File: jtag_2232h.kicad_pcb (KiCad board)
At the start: 2 copper layers, 60 x 25 mm, 90 parts

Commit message: Another import attempt.
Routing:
- added copper zone on F.Cu, net (none)
- removed copper zone on F.Cu, net NetCONN_USB_SHELL

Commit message: Annotated with modified KiCAD
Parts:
- CONN_JTAG: value (none) -> HDR_2x6
- CONN_USB: value (none) -> MICRO_USB_B
- C_BYP_LDO_V1P8: value (none) -> 22nF
- C_EEPROM_VCC, C_EPLD_V1P8_1, C_EPLD_V1P8_2, C_EPLD_VCC_1, C_EPLD_VCC_2, C_FT_CORE_1, C_FT_CORE_2, C_FT_CORE_3, C_FT_VCC_1, C_FT_VCC_2, C_FT_VCC_3, C_FT_VCC_4: value (none) -> 1uF
- C_EPLD_VEIO_1, C_EPLD_VEIO_2, C_OPAMP, C_VEIO_FB: value (none) -> 100nF
- C_FT_OSC_IN, C_FT_OSC_OUT: value (none) -> 4pF
- C_FT_PHY, C_FT_PLL, C_FT_REG_OUT: value (none) -> 3.3uF
- C_IN_LDO_VCC: value (none) -> 2.2uF
- C_OUT_LDO_VCC, C_VEIO_OUT: value (none) -> 10uF
- C_VEIO_CMP: value (none) -> 100pF
- D_JTAG_1, D_JTAG_2, D_JTAG_3, D_JTAG_4, D_JTAG_5: value (none) -> DIODE_2_CC
- EPRG_FT_TCK, EPRG_TCK, EPRG_TDI, EPRG_TDO, EPRG_TMS, GND, UDM, UDN, UGND, V1P8, VBUS, VCC, VCORE, VEIO, VIIO: value (none) -> Test_Point
- LED_FN, LED_PWR: value (none) -> LED_2
- Q_LDO, Q_OV: value (none) -> BJT_PNP
- Q_PWR_LED: value (none) -> MOSFET_P
- Q_TPWR: value (none) -> BJT_NPN
- R_EIO_BYPASS, R_EPRG_EN, R_FT_LDO, R_FT_PHY, R_FT_PLL, R_USB_GND: value (none) -> 0Ohm
- R_EPRG_TCK_PULL, R_PWR_LED_PULL, R_SER_LED_PULL, R_SPI: value (none) -> 10kOhm
- R_FT_REF: value (none) -> 12kOhm
- R_FT_RESET, R_TPWR: value (none) -> 1kOhm
- R_GND_DETECT_PULL: value (none) -> 47kOhm
- R_JTAG_1, R_JTAG_2, R_JTAG_3: value (none) -> 180Ohm
- R_LED_FN, R_LED_PWR: value (none) -> 330Ohm
- R_OUT_LDO_VCC: value (none) -> 2.2Ohm
- R_QBASE: value (none) -> 47Ohm
- R_SPI_DO: value (none) -> 2.2kOhm
- R_VEIO_CMP: value (none) -> 56kOhm
- R_VEIO_DN: value (none) -> 1MOhm
- R_VEIO_FB: value (none) -> 49.9kOhm
- R_VEIO_IN: value (none) -> 200kOhm
- TVS_JTAG_1, TVS_JTAG_2, TVS_JTAG_3: value (none) -> ESD5V0S4US
- U_EEPROM: value (none) -> SPI_EEPROM
- U_EPLD: value (none) -> 5M40Z
- U_FTDI: value (none) -> FT2232H
- U_LDO_V1P8: value (none) -> LDO_SOT23
- U_LDO_VCC: value (none) -> LDO_1117
- U_OPAMP: value (none) -> MCP6001
- Y_FTDI: value (none) -> XTAL_4P
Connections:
- net EPRG_FT_TCK renamed /EPRG_FT_TCK
- net EPRG_TCK renamed /EPRG_TCK
- net EPRG_TDI renamed /EPRG_TDI
- net EPRG_TDO renamed /EPRG_TDO
- net EPRG_TMS renamed /EPRG_TMS
- net FT_GPIO_H0 renamed /FT_GPIO_H0
- net FT_GPIO_H1 renamed /FT_GPIO_H1
- net FT_GPIO_H2 renamed /FT_GPIO_H2
- net FT_GPIO_H3 renamed /FT_GPIO_H3
- net FT_GPIO_H4 renamed /FT_GPIO_H4
- net FT_GPIO_H5 renamed /FT_GPIO_H5
- net FT_GPIO_H6 renamed /FT_GPIO_H6
- net FT_GPIO_H7 renamed /FT_GPIO_H7
- net FT_GPIO_L0 renamed /FT_GPIO_L0
- net FT_GPIO_L1 renamed /FT_GPIO_L1
- net FT_GPIO_L2 renamed /FT_GPIO_L2
- net FT_JTAG_EN_N renamed /FT_JTAG_EN_N
- net FT_JTAG_RTCK renamed /FT_JTAG_RTCK
- net FT_JTAG_TCK renamed /FT_JTAG_TCK
- net FT_JTAG_TDI renamed /FT_JTAG_TDI
- net FT_JTAG_TDO renamed /FT_JTAG_TDO
- net FT_JTAG_TMS renamed /FT_JTAG_TMS
- net FT_SER_LED renamed /FT_SER_LED
- net FT_SER_RXD renamed /FT_SER_RXD
- net FT_SER_TXD renamed /FT_SER_TXD
- net GND_DETECT renamed /GND_DETECT
- net JTAG_RST renamed /JTAG_RST
- net JTAG_RTCK renamed /JTAG_RTCK
- net JTAG_TCK renamed /JTAG_TCK
- net JTAG_TDI renamed /JTAG_TDI
- net JTAG_TDO renamed /JTAG_TDO
- net JTAG_TMS renamed /JTAG_TMS
- net LED_ACT renamed /LED_ACT
- net LED_NO_TGT renamed /LED_NO_TGT
- net NetCONN_USB_SHELL renamed Net-(CONN_USB-PadSHELL)
- net NetC_BYP_LDO_V1P8_2 renamed Net-(U_LDO_V1P8-BYP)
- net NetC_FT_OSC_IN_1 renamed Net-(U_FTDI-OSCI)
- net NetC_FT_OSC_OUT_1 renamed Net-(U_FTDI-OSCO)
- net NetC_FT_PHY_1 renamed Net-(U_FTDI-VPHY)
- net NetC_FT_PLL_1 renamed Net-(U_FTDI-VPLL)
- net NetC_OUT_LDO_VCC_2 renamed Net-(C_OUT_LDO_VCC-Pad2)
- net NetC_VEIO_CMP_1 renamed Net-(C_VEIO_CMP-Pad1)
- net NetC_VEIO_CMP_2 renamed Net-(U_OPAMP-Vout)
- net NetC_VEIO_FB_1 renamed Net-(U_OPAMP-+)
- net NetD_JTAG_1_A2 renamed Net-(D_JTAG_1-PadA2)
- net NetD_JTAG_2_A1 renamed Net-(D_JTAG_2-PadA1)
- net NetD_JTAG_2_A2 renamed Net-(D_JTAG_2-PadA2)
- net NetD_JTAG_3_A1 renamed Net-(D_JTAG_3-PadA1)
- net NetD_JTAG_3_A2 renamed Net-(D_JTAG_3-PadA2)
- net NetD_JTAG_4_A1 renamed Net-(D_JTAG_4-PadA1)
- net NetD_JTAG_4_A2 renamed Net-(D_JTAG_4-PadA2)
- net NetD_JTAG_5_A1 renamed Net-(D_JTAG_5-PadA1)
- net NetD_JTAG_5_A2 renamed Net-(D_JTAG_5-PadA2)
- net NetLED_FN_A1 renamed Net-(LED_FN-PadA1)
- net NetLED_FN_A2 renamed Net-(LED_FN-PadA2)
- net NetLED_PWR_A1 renamed Net-(LED_PWR-PadA1)
- net NetLED_PWR_A2 renamed Net-(LED_PWR-PadA2)
- net NetQ_LDO_B renamed Net-(Q_LDO-PadB)
- net NetQ_OV_B renamed Net-(Q_OV-PadB)
- net NetQ_PWR_LED_D renamed Net-(Q_PWR_LED-PadD)
- net NetQ_TPWR_B renamed Net-(Q_TPWR-PadB)
- net NetQ_TPWR_E renamed Net-(Q_TPWR-PadE)
- net NetR_FT_REF_2 renamed Net-(U_FTDI-REF)
- net NetR_FT_RESET_1 renamed Net-(U_FTDI-RESET#)
- net NetR_SPI_2 renamed Net-(U_EEPROM-D_IN)
- net NetR_SPI_3 renamed Net-(U_EEPROM-SCLK)
- net NetR_SPI_4 renamed Net-(U_EEPROM-CS_N)
- net NetR_SPI_DO_1 renamed Net-(U_EEPROM-D_OUT)
- net NetR_VEIO_CMP_1 renamed Net-(U_OPAMP--)
- net SER_RXD renamed /SER_RXD
- net SER_TXD renamed /SER_TXD
- net USB_DM renamed /USB_DM
- net USB_DP renamed /USB_DP
- CONN_USB pad 4: (no net) -> unconnected-(CONN_USB-ID-Pad4)
- D_JTAG_1 pad A1: (no net) -> unconnected-(D_JTAG_1-PadA1)
- R_SPI pad 1: (no net) -> unconnected-(R_SPI-Pad1)
- TVS_JTAG_3 pad 1: (no net) -> unconnected-(TVS_JTAG_3-K-Pad1)
- TVS_JTAG_3 pad 3: (no net) -> unconnected-(TVS_JTAG_3-K-Pad3)
- TVS_JTAG_3 pad 4: (no net) -> unconnected-(TVS_JTAG_3-K-Pad4)
- U_EPLD pad 25: (no net) -> unconnected-(U_EPLD-I/O-Pad25)
- U_EPLD pad 26: (no net) -> unconnected-(U_EPLD-I/O-Pad26)
- U_EPLD pad 27: (no net) -> unconnected-(U_EPLD-I/O-Pad27)
- U_EPLD pad 28: (no net) -> unconnected-(U_EPLD-I/O-Pad28)
- U_EPLD pad 34: (no net) -> unconnected-(U_EPLD-I/O-Pad34)
- U_EPLD pad 35: (no net) -> unconnected-(U_EPLD-I/O-Pad35)
- U_EPLD pad 36: (no net) -> unconnected-(U_EPLD-I/O-Pad36)
- U_EPLD pad 37: (no net) -> unconnected-(U_EPLD-I/O-Pad37)
- U_EPLD pad 38: (no net) -> unconnected-(U_EPLD-I/O-Pad38)
- U_EPLD pad 40: (no net) -> unconnected-(U_EPLD-I/O-Pad40)
- U_EPLD pad 50: (no net) -> unconnected-(U_EPLD-I/O-Pad50)
- U_EPLD pad 51: (no net) -> unconnected-(U_EPLD-I/O-Pad51)
- U_EPLD pad 52: (no net) -> unconnected-(U_EPLD-I/O-Pad52)
- U_EPLD pad 53: (no net) -> unconnected-(U_EPLD-I/O-Pad53)
- U_EPLD pad 54: (no net) -> unconnected-(U_EPLD-I/O-Pad54)
- U_EPLD pad 55: (no net) -> unconnected-(U_EPLD-I/O-Pad55)
- U_EPLD pad 56: (no net) -> unconnected-(U_EPLD-I/O-Pad56)
- U_EPLD pad 58: (no net) -> unconnected-(U_EPLD-I/O-Pad58)
- U_EPLD pad 59: (no net) -> unconnected-(U_EPLD-I/O-Pad59)
- U_EPLD pad 60: (no net) -> unconnected-(U_EPLD-I/O-Pad60)
- U_EPLD pad 61: (no net) -> unconnected-(U_EPLD-I/O-Pad61)
- U_EPLD pad 62: (no net) -> unconnected-(U_EPLD-I/O-Pad62)
- U_EPLD pad 63: (no net) -> unconnected-(U_EPLD-I/O-Pad63)
- U_FTDI pad 36: (no net) -> unconnected-(U_FTDI-SUSPEND#-Pad36)
- U_FTDI pad 40: (no net) -> unconnected-(U_FTDI-BDBUS2-Pad40)
- U_FTDI pad 41: (no net) -> unconnected-(U_FTDI-BDBUS3-Pad41)
- U_FTDI pad 43: (no net) -> unconnected-(U_FTDI-BDBUS4-Pad43)
- U_FTDI pad 44: (no net) -> unconnected-(U_FTDI-BDBUS5-Pad44)
- U_FTDI pad 45: (no net) -> unconnected-(U_FTDI-BDBUS6-Pad45)
- U_FTDI pad 46: (no net) -> unconnected-(U_FTDI-BDBUS7-Pad46)
- U_FTDI pad 48: (no net) -> unconnected-(U_FTDI-BCBUS0-Pad48)
- U_FTDI pad 52: (no net) -> unconnected-(U_FTDI-BCBUS1-Pad52)

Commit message: Cleared all DRCs, mostly fixed up library.
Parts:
- added LOGO1: ~, jtag_2232h:MC_logo_micro, F.Cu at (145.5, 112.4)
- CONN_USB1: renamed from CONN_USB; value MICRO_USB_B -> (none)
- moved R_VEIO_DN1 0.81 mm to (143.4, 110.2)
- renumbered CONN_JTAG to CONN_JTAG1, C_EEPROM_VCC to C_EEPROM_VCC1, C_FT_OSC_IN to C_FT_OSC_IN1, C_FT_OSC_OUT to C_FT_OSC_OUT1, C_FT_PHY to C_FT_PHY1, C_FT_PLL to C_FT_PLL1, C_FT_REG_OUT to C_FT_REG_OUT1, C_IN_LDO_VCC to C_IN_LDO_VCC1, C_OPAMP to C_OPAMP1, C_OUT_LDO_VCC to C_OUT_LDO_VCC1, C_VEIO_CMP to C_VEIO_CMP1, C_VEIO_FB to C_VEIO_FB1, C_VEIO_OUT to C_VEIO_OUT1, EPRG_FT_TCK to EPRG_FT_TCK1, EPRG_TCK to EPRG_TCK1, EPRG_TDI to EPRG_TDI1, EPRG_TDO to EPRG_TDO1, EPRG_TMS to EPRG_TMS1, GND to GND1, LED_FN to LED_FN1, LED_PWR to LED_PWR1, Q_LDO to Q_LDO1, Q_OV to Q_OV1, Q_PWR_LED to Q_PWR_LED1, Q_TPWR to Q_TPWR1, R_EIO_BYPASS to R_EIO_BYPASS1, R_EPRG_EN to R_EPRG_EN1, R_EPRG_TCK_PULL to R_EPRG_TCK_PULL1, R_FT_LDO to R_FT_LDO1, R_FT_PHY to R_FT_PHY1, R_FT_PLL to R_FT_PLL1, R_FT_REF to R_FT_REF1, R_FT_RESET to R_FT_RESET1, R_GND_DETECT_PULL to R_GND_DETECT_PULL1, R_LED_FN to R_LED_FN1, R_LED_PWR to R_LED_PWR1, R_OUT_LDO_VCC to R_OUT_LDO_VCC1, R_PWR_LED_PULL to R_PWR_LED_PULL1, R_QBASE to R_QBASE1, R_SER_LED_PULL to R_SER_LED_PULL1, R_SPI to R_SPI1, R_SPI_DO to R_SPI_DO1, R_TPWR to R_TPWR1, R_USB_GND to R_USB_GND1, R_VEIO_CMP to R_VEIO_CMP1, R_VEIO_DN to R_VEIO_DN1, R_VEIO_FB to R_VEIO_FB1, R_VEIO_IN to R_VEIO_IN1, UDM to UDM1, UDN to UDN1, UGND to UGND1, U_EEPROM to U_EEPROM1, U_EPLD to U_EPLD1, U_FTDI to U_FTDI1, U_LDO_VCC to U_LDO_VCC1, U_OPAMP to U_OPAMP1, VBUS to VBUS1, VCC to VCC1, VCORE to VCORE1, VEIO to VEIO1, VIIO to VIIO1, Y_FTDI to Y_FTDI1
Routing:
- net VCC_IO: track 28.6 -> 29.3 mm
- net VCC_EIO: track 54.0 -> 53.4 mm
- net VCC_FT_CORE: vias 5 -> 4
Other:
- rule pad_to_mask_clearance: 0.1016 -> 0

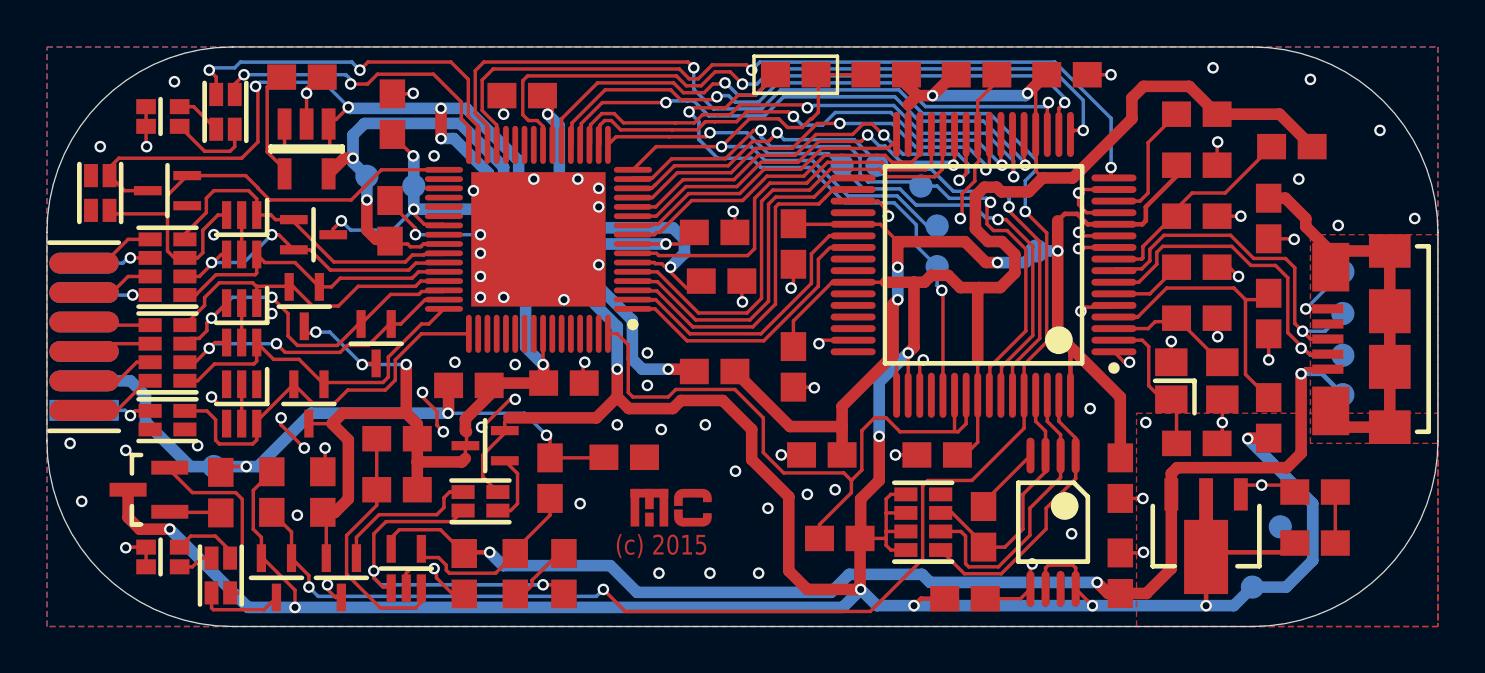
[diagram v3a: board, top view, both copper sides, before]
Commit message: Now using USB-C connector.
Also using much more KiCAD-like components.
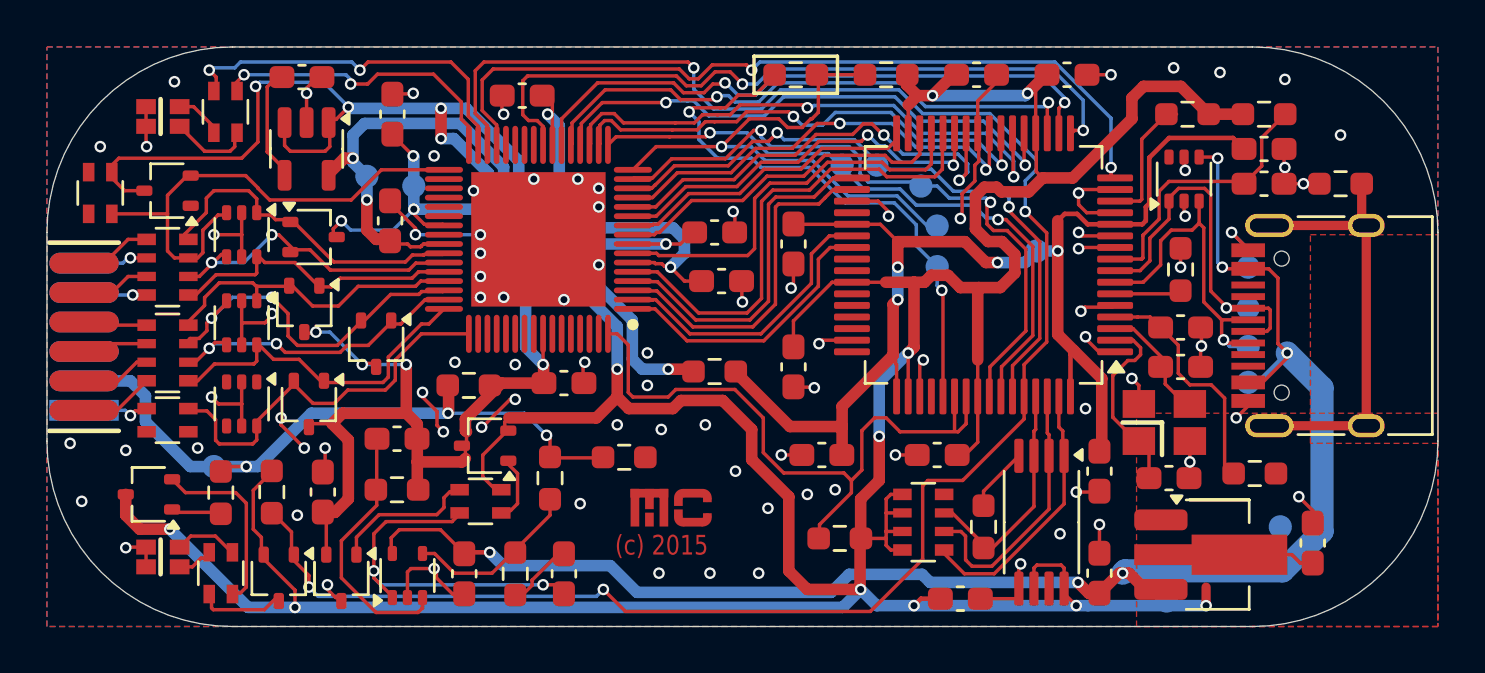
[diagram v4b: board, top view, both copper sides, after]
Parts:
- removed CONN_USB1: , jtag_2232h:MICRO_USB_B
- removed D_JTAG_1, D_JTAG_2, D_JTAG_3, D_JTAG_4, D_JTAG_5: DIODE_2_CC, jtag_2232h:SOT65P210X110_3N_2DIODE_CC
- removed Q_LDO1, Q_OV1: BJT_PNP, jtag_2232h:SOT65P210X110_3N_BJT_BEC
- removed Q_PWR_LED1: MOSFET_P, jtag_2232h:SOT65P210X110_3N_FET_GSD
- removed Q_TPWR1: BJT_NPN, jtag_2232h:SOT95P237X112_3N_BJT_BEC
- removed R_OUT_LDO_VCC1: 2.2Ohm, jtag_2232h:M1608
- removed U_OPAMP1: MCP6001, jtag_2232h:SOT65P210X110_5N
- added D2: BAV70W, Package_TO_SOT_SMD:SOT-323_SC-70, F.Cu at (123.7, 98.7)
- added D3: BAV70W, Package_TO_SOT_SMD:SOT-323_SC-70, F.Cu at (130.0, 100.7)
- added D4: BAV70W, Package_TO_SOT_SMD:SOT-323_SC-70, F.Cu at (129.6, 103.8)
- added D5: BAV70W, Package_TO_SOT_SMD:SOT-323_SC-70, F.Cu at (132.7, 105.3)
- added D6: BAV70W, Package_TO_SOT_SMD:SOT-323_SC-70, F.Cu at (129.8, 107.9)
- added J1: USB_C_Receptacle_USB2.0_14P, Connector_USB:USB_C_Receptacle_HRO_TYPE-C-31-M-12, F.Cu at (174.4, 104.5)
- added Q1: BC848W, Package_TO_SOT_SMD:SOT-323_SC-70, F.Cu at (122.9, 111.8)
- added Q2: BC807W, Package_TO_SOT_SMD:SOT-323_SC-70, F.Cu at (131.2, 115.4)
- added Q3: BC807W, Package_TO_SOT_SMD:SOT-323_SC-70, F.Cu at (137.4, 109.7)
- added Q4: BSS84AKW, Package_TO_SOT_SMD:SOT-323_SC-70, F.Cu at (128.5, 115.4)
- added TVS_JTAG_4: ESD5V0S4US, Package_TO_SOT_SMD:SOT-363_SC-70-6, F.Cu at (167.6, 98.2)
- added U1: MCP6001x-LT, Package_TO_SOT_SMD:SOT-353_SC-70-5, F.Cu at (134.1, 115.3)
- CONN_JTAG1: footprint jtag_2232h:RCP_1P27_2X6_EDGE -> jtag_ft2232h:RCP_1P27_2X6_EDGE
- C_BYP_LDO_V1P8, C_EEPROM_VCC1, C_EPLD_V1P8_1, C_EPLD_V1P8_2, C_EPLD_VCC_1, C_EPLD_VCC_2, C_EPLD_VEIO_1, C_EPLD_VEIO_2, C_FT_CORE_1, C_FT_CORE_2, C_FT_CORE_3, C_FT_OSC_IN1, C_FT_OSC_OUT1, C_FT_PHY1, C_FT_PLL1, C_FT_REG_OUT1, C_FT_VCC_1, C_FT_VCC_2, C_FT_VCC_3, C_FT_VCC_4, C_IN_LDO_VCC1, C_OPAMP1, C_OUT_LDO_VCC1, C_VEIO_CMP1, C_VEIO_FB1, C_VEIO_OUT1: footprint jtag_2232h:M1608 -> Capacitor_SMD:C_0603_1608Metric_Pad1.08x0.95mm_HandSolder
- EPRG_FT_TCK1, EPRG_TCK1, EPRG_TDI1, EPRG_TDO1, EPRG_TMS1, GND1, UDM1, UDN1, UGND1, V1P8, VBUS1, VCC1, VCORE1, VEIO1, VIIO1: footprint jtag_2232h:TEST_POINT_100 -> jtag_ft2232h:TEST_POINT_100
- LED_FN1, LED_PWR1: footprint jtag_2232h:LEDX2_150X160X55 -> jtag_ft2232h:LEDX2_150X160X55
- LOGO1: footprint jtag_2232h:MC_logo_micro -> jtag_ft2232h:MC_logo_micro
- R_EIO_BYPASS1, R_EPRG_EN1, R_EPRG_TCK_PULL1, R_FT_LDO1, R_FT_PHY1, R_FT_PLL1, R_FT_REF1, R_FT_RESET1, R_PWR_LED_PULL1, R_SER_LED_PULL1, R_SPI_DO1, R_TPWR1, R_USB_GND1, R_VEIO_CMP1, R_VEIO_DN1, R_VEIO_FB1, R_VEIO_IN1: footprint jtag_2232h:M1608 -> Resistor_SMD:R_0603_1608Metric_Pad0.98x0.95mm_HandSolder
- R_GND_DETECT_PULL1, R_JTAG_3, R_LED_FN1, R_LED_PWR1, R_QBASE1: footprint jtag_2232h:M1608x2 -> Resistor_SMD:R_Array_Convex_2x0603
- R_JTAG_1, R_JTAG_2, R_SPI1: footprint jtag_2232h:M1608x4 -> Resistor_SMD:R_Array_Convex_4x0603
- TVS_JTAG_1, TVS_JTAG_2, TVS_JTAG_3: footprint jtag_2232h:SOT65P210X110_6N -> Package_TO_SOT_SMD:SOT-363_SC-70-6
- U_EEPROM1: footprint jtag_2232h:TSSOP8 -> Package_SO:TSSOP-8_4.4x3mm_P0.65mm
- U_EPLD1: footprint jtag_2232h:TSQFP40P900X900X120_HS_64N -> jtag_ft2232h:TSQFP40P900X900X120_HS_64N
- U_FTDI1: footprint jtag_2232h:TSQFP50P1200X1200X120_64M -> Package_QFP:LQFP-64_10x10mm_P0.5mm
- U_LDO_V1P8: footprint jtag_2232h:SOT95P255X145_5N -> Package_TO_SOT_SMD:SOT-23-5
- U_LDO_VCC1: footprint jtag_2232h:SOT89-150P410X160-3N -> Package_TO_SOT_SMD:SOT-89-3_Handsoldering
- Y_FTDI1: footprint jtag_2232h:XTAL_4P_3P2x2P5 -> jtag_ft2232h:XTAL_4P_3P2x2P5
- moved VBUS1 4.12 mm to (170.3, 107.0)
- moved UDM1 4.10 mm to (170.3, 105.4)
- moved UDN1 4.09 mm to (170.3, 103.8)
- moved UGND1 4.09 mm to (170.3, 102.0)
- moved C_FT_PHY1 3.85 mm to (167.4, 104.6), turned to 0 degrees
- moved VCC1 3.75 mm to (166.8, 116.4)
- moved R_USB_GND1 3.44 mm to (174.3, 98.4), turned to 0 degrees
- moved C_FT_PLL1 3.22 mm to (171.0, 98.4)
- moved C_FT_CORE_1 2.98 mm to (171.0, 96.9)
- moved R_FT_PHY1 2.47 mm to (170.6, 110.9), turned to 0 degrees
- moved Y_FTDI1 2.28 mm to (166.7, 108.7)
- moved C_FT_OSC_OUT1 2.21 mm to (167.4, 106.3)
- moved C_FT_OSC_IN1 1.92 mm to (166.9, 111.1)
- moved R_FT_PLL1 1.84 mm to (171.0, 95.4), turned to 180 degrees
- moved C_FT_CORE_3 0.95 mm to (163.9, 110.8)
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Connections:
- C_OUT_LDO_VCC1 pad 2: Net-(C_OUT_LDO_VCC1-Pad2) -> GND
- C_VEIO_CMP1 pad 2: Net-(U_OPAMP1-Vout) -> Net-(C_VEIO_CMP1-Pad2)
- R_GND_DETECT_PULL1 pad 1: Net-(D_JTAG_1-PadA2) -> VCC
- R_GND_DETECT_PULL1 pad 4: VCC -> Net-(D2-A-Pad2)
- R_JTAG_1 pad 1: Net-(D_JTAG_2-PadA1) -> Net-(D4-A-Pad1)
- R_JTAG_1 pad 2: Net-(D_JTAG_1-PadA2) -> Net-(D3-A-Pad2)
- R_JTAG_1 pad 3: Net-(D_JTAG_2-PadA2) -> Net-(D2-A-Pad2)
- R_JTAG_1 pad 4: Net-(D_JTAG_3-PadA1) -> Net-(D3-A-Pad1)
- R_JTAG_1 pad 5: /JTAG_RTCK -> /JTAG_RST
- R_JTAG_1 pad 6: /JTAG_TDI -> /GND_DETECT
- R_JTAG_1 pad 7: /GND_DETECT -> /JTAG_TDI
- R_JTAG_1 pad 8: /JTAG_RST -> /JTAG_RTCK
- R_JTAG_2 pad 1: Net-(D_JTAG_3-PadA2) -> Net-(D6-A-Pad1)
- R_JTAG_2 pad 2: Net-(D_JTAG_4-PadA2) -> Net-(D5-A-Pad1)
- R_JTAG_2 pad 3: Net-(D_JTAG_4-PadA1) -> Net-(D5-A-Pad2)
- R_JTAG_2 pad 4: Net-(D_JTAG_5-PadA1) -> Net-(D4-A-Pad2)
- R_JTAG_2 pad 5: /SER_TXD -> /JTAG_TDO
- R_JTAG_2 pad 6: /JTAG_TMS -> /JTAG_TCK
- R_JTAG_2 pad 7: /JTAG_TCK -> /JTAG_TMS
- R_JTAG_2 pad 8: /JTAG_TDO -> /SER_TXD
- R_JTAG_3 pad 1: Net-(D_JTAG_5-PadA2) -> /SER_RXD
- R_JTAG_3 pad 4: /SER_RXD -> Net-(D6-A-Pad2)
- R_LED_FN1 pad 1: Net-(LED_FN1-PadA1) -> Net-(LED_FN1-PadA2)
- R_LED_FN1 pad 2: Net-(LED_FN1-PadA2) -> Net-(LED_FN1-PadA1)
- R_LED_FN1 pad 3: /LED_ACT -> /LED_NO_TGT
- R_LED_FN1 pad 4: /LED_NO_TGT -> /LED_ACT
- R_LED_PWR1 pad 1: Net-(LED_PWR1-PadA1) -> Net-(LED_PWR1-PadA2)
- R_LED_PWR1 pad 2: Net-(LED_PWR1-PadA2) -> Net-(LED_PWR1-PadA1)
- R_QBASE1 pad 1: Net-(U_OPAMP1-Vout) -> Net-(Q2-B)
- R_QBASE1 pad 2: Net-(Q_OV1-PadB) -> Net-(C_VEIO_CMP1-Pad2)
- R_QBASE1 pad 3: VCC -> Net-(Q3-B)
- R_QBASE1 pad 4: Net-(Q_LDO1-PadB) -> VCC
- R_SPI1 pad 1: unconnected-(R_SPI1-Pad1) -> Net-(U_EEPROM1-CS_N)
- R_SPI1 pad 2: Net-(U_EEPROM1-D_IN) -> Net-(U_EEPROM1-SCLK)
- R_SPI1 pad 3: Net-(U_EEPROM1-SCLK) -> Net-(U_EEPROM1-D_IN)
- R_SPI1 pad 4: Net-(U_EEPROM1-CS_N) -> unconnected-(R_SPI1-Pad4)
- TVS_JTAG_1 pad 1: Net-(D_JTAG_2-PadA1) -> Net-(D3-A-Pad1)
- TVS_JTAG_1 pad 3: Net-(D_JTAG_1-PadA2) -> Net-(D2-A-Pad2)
- TVS_JTAG_1 pad 4: Net-(D_JTAG_2-PadA2) -> Net-(D3-A-Pad2)
- TVS_JTAG_1 pad 6: Net-(D_JTAG_3-PadA1) -> Net-(D4-A-Pad1)
- TVS_JTAG_2 pad 1: Net-(D_JTAG_3-PadA2) -> Net-(D4-A-Pad2)
- TVS_JTAG_2 pad 3: Net-(D_JTAG_4-PadA2) -> Net-(D5-A-Pad2)
- TVS_JTAG_2 pad 4: Net-(D_JTAG_4-PadA1) -> Net-(D5-A-Pad1)
- TVS_JTAG_2 pad 6: Net-(D_JTAG_5-PadA1) -> Net-(D6-A-Pad1)
- TVS_JTAG_3 pad 6: Net-(D_JTAG_5-PadA2) -> Net-(D6-A-Pad2)
- U_EPLD1 pad 33: Net-(D_JTAG_1-PadA2) -> Net-(D2-A-Pad2)
- U_EPLD1 pad 42: Net-(D_JTAG_2-PadA1) -> Net-(D3-A-Pad1)
- U_EPLD1 pad 43: Net-(D_JTAG_2-PadA2) -> Net-(D3-A-Pad2)
- U_EPLD1 pad 44: Net-(D_JTAG_3-PadA1) -> Net-(D4-A-Pad1)
- U_EPLD1 pad 45: Net-(D_JTAG_3-PadA2) -> Net-(D4-A-Pad2)
- U_EPLD1 pad 46: Net-(D_JTAG_4-PadA2) -> Net-(D5-A-Pad2)
- U_EPLD1 pad 47: Net-(D_JTAG_4-PadA1) -> Net-(D5-A-Pad1)
- U_EPLD1 pad 48: Net-(D_JTAG_5-PadA1) -> Net-(D6-A-Pad1)
- U_EPLD1 pad 49: Net-(D_JTAG_5-PadA2) -> Net-(D6-A-Pad2)
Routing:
- net Net-(D_JTAG_1-PadA2): track 22.2 -> 0.00 mm
- net Net-(D2-A-Pad2): track 0.00 -> 22.2 mm
- net Net-(D_JTAG_5-PadA2): track 17.0 -> 0.00 mm
- net Net-(D6-A-Pad2): track 0.00 -> 17.0 mm
- net VCC: track 255.7 -> 238.9 mm, vias 18 -> 17
- net VCC_VBUS: track 53.4 -> 70.1 mm, vias 3 -> 6
- net Net-(C_VEIO_CMP1-Pad2): track 0.00 -> 16.1 mm, vias 0 -> 2
- net Net-(U_OPAMP1-Vout): track 15.9 -> 0.00 mm, vias 2 -> 0
- net Net-(D_JTAG_4-PadA2): track 15.6 -> 0.00 mm, vias 2 -> 0
- net Net-(D5-A-Pad2): track 0.00 -> 15.6 mm, vias 0 -> 2
- net Net-(D_JTAG_5-PadA1): track 14.9 -> 0.00 mm
- net Net-(D6-A-Pad1): track 0.00 -> 14.9 mm
- net Net-(D_JTAG_2-PadA1): track 14.4 -> 0.00 mm
- net Net-(D3-A-Pad1): track 0.00 -> 14.4 mm
- net Net-(D_JTAG_3-PadA2): track 13.7 -> 0.00 mm
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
